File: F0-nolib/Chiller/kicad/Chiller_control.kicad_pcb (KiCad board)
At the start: 2 copper layers, 62 x 60.5 mm, 57 parts, among them J1 DB9_Female, J2 12VIN, J3 Ext. devices, J4 Tsens, J5 Cooler, J6 Heater, J7 Pump, Q1 SI2300, Q2 SI2300, Q3 SI2300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

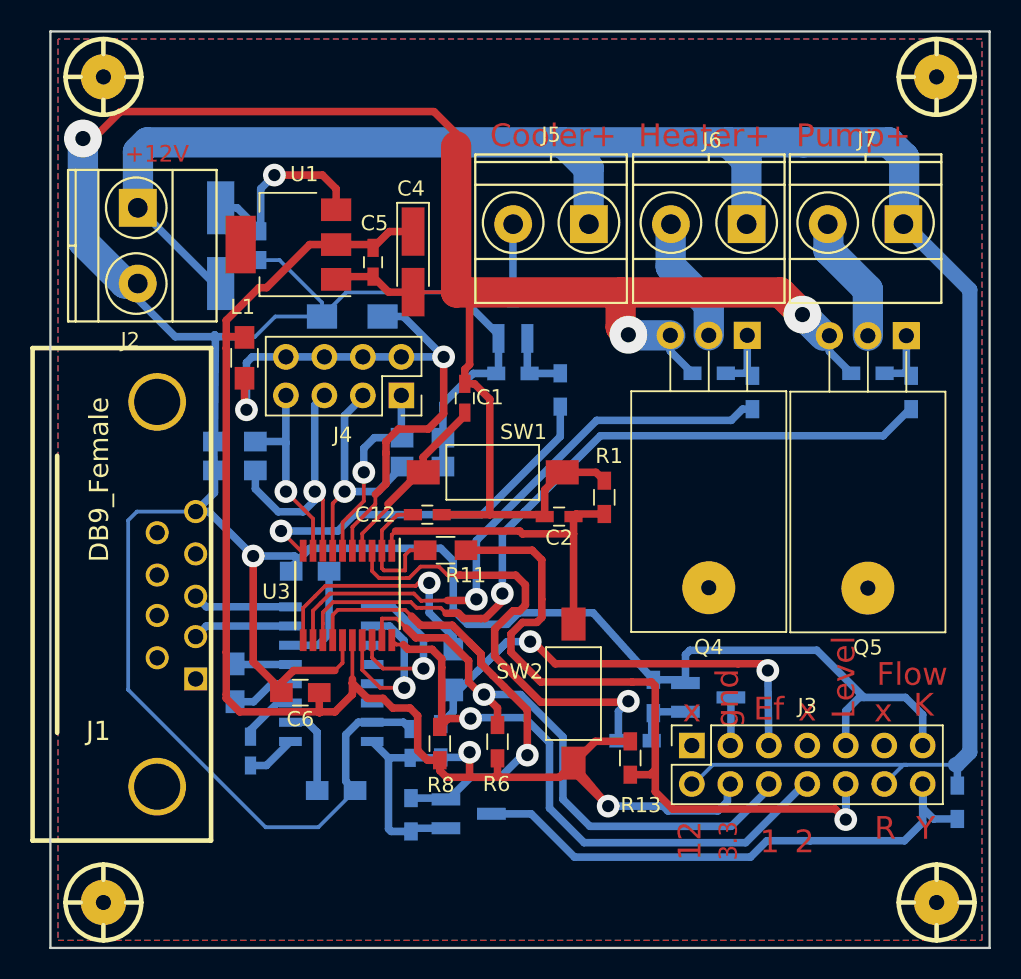
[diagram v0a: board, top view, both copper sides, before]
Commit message: Change chiller schematics: fix bugs, prepare for manufacture production
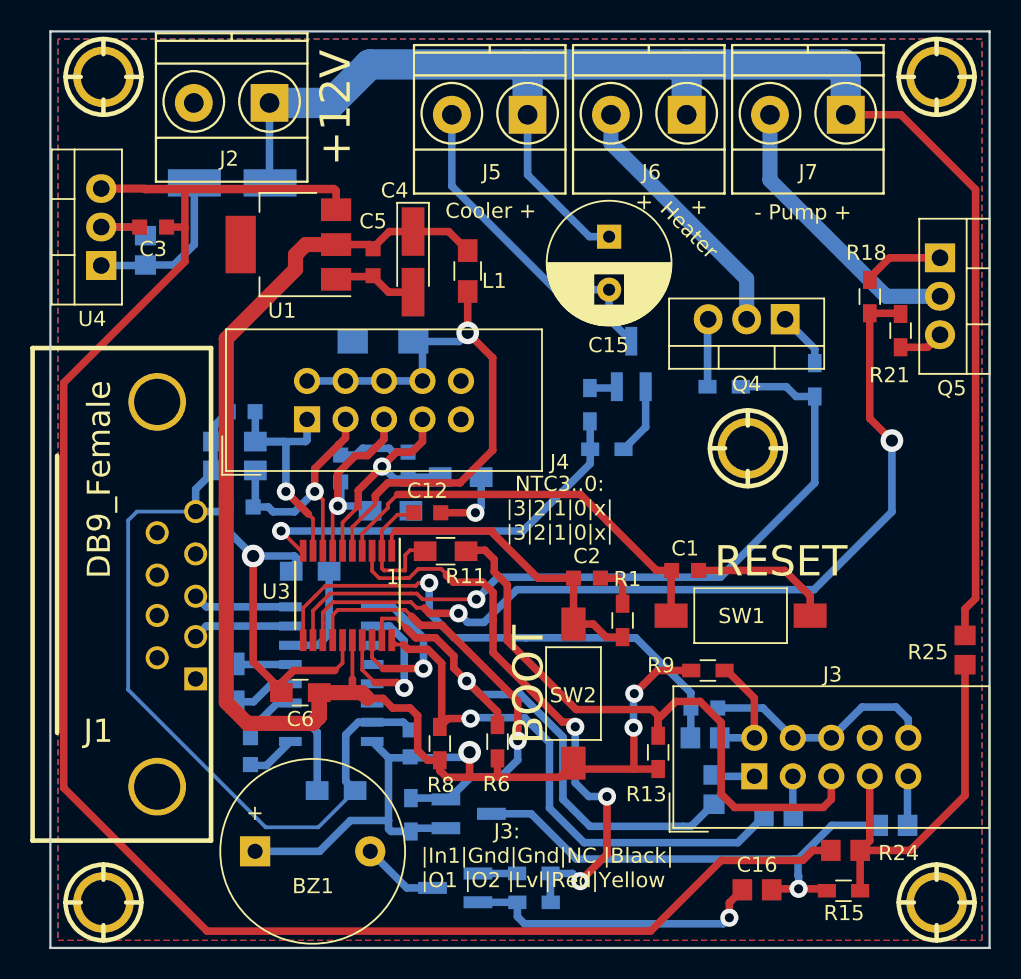
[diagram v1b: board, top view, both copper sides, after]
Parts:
- added BZ1: Buzzer, Buzzer_Beeper:Buzzer_12x9.5RM7.6, F.Cu at (55.9, 88.2)
- added C14: 1u, Capacitor_SMD:C_0805_2012Metric_Pad1.29x1.40mm_HandSolder, B.Cu at (48.6, 48.5)
- added C15: 100u, Capacitor_THT:CP_Radial_D8.0mm_P3.50mm, F.Cu at (79.2, 47.6)
- added C16: 1u, Capacitor_SMD:C_0805_2012Metric_Pad1.29x1.40mm_HandSolder, F.Cu at (89.0, 90.7)
- added C17: 0.1, Capacitor_SMD:C_0603_1608Metric_Pad0.99x1.00mm_HandSolder, B.Cu at (66.0, 62.7)
- added C18: 0.1, Capacitor_SMD:C_0603_1608Metric_Pad0.99x1.00mm_HandSolder, B.Cu at (55.0, 59.1)
- added C19: 0.1, Capacitor_SMD:C_0603_1608Metric_Pad0.99x1.00mm_HandSolder, B.Cu at (61.5, 62.9)
- added C20: 0.1, Capacitor_SMD:C_0603_1608Metric_Pad0.99x1.00mm_HandSolder, B.Cu at (54.8, 65.4)
- added C21: 0.1, Capacitor_SMD:C_0603_1608Metric_Pad0.99x1.00mm_HandSolder, B.Cu at (85.5, 78.7)
- added R22: 220, Resistor_SMD:R_0805_2012Metric_Pad1.29x1.40mm_HandSolder, B.Cu at (86.2, 84.1)
- added R23: 220, Resistor_SMD:R_0805_2012Metric_Pad1.29x1.40mm_HandSolder, B.Cu at (90.4, 85.8)
- added R24: 0, Resistor_SMD:R_0805_2012Metric_Pad1.29x1.40mm_HandSolder, F.Cu at (94.8, 88.1)
- added R25: 0, Resistor_SMD:R_0805_2012Metric_Pad1.29x1.40mm_HandSolder, F.Cu at (102.7, 74.9)
- added R26: 220, Resistor_SMD:R_0805_2012Metric_Pad1.29x1.40mm_HandSolder, B.Cu at (98.0, 86.4)
- added U4: L7805, TO_SOT_Packages_THT:TO-220-3_Vertical, F.Cu at (45.7, 49.5)
- added hole_3mm: Val**, modules:hole_3mm, F.Cu at (88.4, 61.5)
- C1, C12, C2, C5, C8, C9: footprint Capacitor_SMD.pretty:C_0603_HandSoldering -> Capacitor_SMD:C_0603_1608Metric_Pad0.99x1.00mm_HandSolder
- C3: footprint Capacitor_SMD.pretty:C_0603_HandSoldering -> Capacitor_SMD:C_0603_1608Metric_Pad0.99x1.00mm_HandSolder; moved to F.Cu
- J3: value Ext. devices -> DC3-10P; footprint Connector_PinSocket_2.54mm:PinSocket_2x07_P2.54mm_Vertical -> Connector_IDC:IDC-Header_2x05_P2.54mm_Vertical
- J4: value Tsens -> DC3-10P; footprint Connector_PinSocket_2.54mm:PinSocket_2x04_P2.54mm_Vertical -> Connector_IDC:IDC-Header_2x05_P2.54mm_Vertical
- Q4, Q5: footprint TO_SOT_Packages_THT:TO-220_Horizontal -> TO_SOT_Packages_THT:TO-220-3_Vertical
- R11: value 47 -> 220
- R15, R18, R21, R9: moved to F.Cu
- R7: value 47 -> 220; footprint Resistors_SMD.pretty:R_0805_HandSoldering -> Resistor_SMD:R_0805_2012Metric_Pad1.29x1.40mm_HandSolder
- moved Q1 20.9 mm to (69.1, 90.6), turned to 180 degrees
- moved SW1 18.9 mm to (87.9, 72.6)
- moved C1 18.5 mm to (84.3, 69.6), turned to 0 degrees
- moved R9 18.2 mm to (85.8, 76.2), turned to 0 degrees
- moved R7 17.2 mm to (85.6, 80.7), turned to 180 degrees
- moved L1 15.8 mm to (69.9, 49.8)
- moved R12 15.7 mm to (74.3, 91.5), turned to 0 degrees
- moved J2 11.1 mm to (56.8, 38.7), turned to 180 degrees
- moved R10 11.0 mm to (74.3, 89.6), turned to 0 degrees
- moved R15 9.52 mm to (94.7, 90.8), turned to 180 degrees
- moved Q3 8.44 mm to (80.7, 56.0)
- moved J5 8.28 mm to (73.9, 39.5)
- moved J6 8.24 mm to (84.4, 39.5)
- moved R1 8.22 mm to (80.1, 72.9)
- moved J7 8.17 mm to (94.9, 39.5)
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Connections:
- C3 pad 1: Net-(C3-Pad1) -> +5V
- D1 pad 1: Net-(C3-Pad1) -> Net-(C14-Pad1)
- J3 pad 1: (no net) -> /Out1
- J3 pad 10: /W.levl -> GND
- J3 pad 2: +12V -> /IN
- J3 pad 3: /Alrm -> /Out2
- J3 pad 4: +3V3 -> GND
- J3 pad 5: /EF -> /W.levl
- J3 pad 6: /DigOut1 -> GND
- J3 pad 7: (no net) -> /Red
- J3 pad 8: /DigOut2 -> (no net)
- J3 pad 9: GND -> /Yellow
- J4 pad 1: /ADC0 -> /ADC3
- J4 pad 3: /ADC1 -> /ADC2
- J4 pad 5: /ADC2 -> /ADC1
- J4 pad 7: /ADC3 -> /ADC0
- Q1 pad 3: /Alrm -> Net-(BZ1-Pad2)
- Q2 pad 3: /Yellow -> Net-(C16-Pad2)
- R12 pad 2: Net-(Q1-Pad1) -> /DigOut0
- R15 pad 1: +12V -> /Red
- R15 pad 2: /Yellow -> Net-(C16-Pad2)
- R19 pad 2: Net-(Q3-Pad1) -> /Tim14Ch1
- R20 pad 2: Net-(Q4-Pad1) -> /TIM16_Ch1
- R21 pad 2: Net-(Q5-Pad1) -> /TIM17_Ch1
- R7 pad 1: /EF -> /IN
- R9 pad 2: /EF -> /IN
- U1 pad 3: Net-(C3-Pad1) -> +5V
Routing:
- net GND: track 309.7 -> 157.0 mm, vias 4 -> 3
- net +5V: track 0.00 -> 133.2 mm
- net /Yellow: track 37.3 -> 3.26 mm
- net Net-(C16-Pad2): track 0.00 -> 33.4 mm, vias 0 -> 1
- net /EF: track 33.2 -> 0.00 mm, vias 2 -> 0
- net +12V: track 138.2 -> 105.8 mm
- net /Red: track 0.00 -> 24.9 mm
- net /DigIn1: track 16.2 -> 36.5 mm
- net Net-(C15-Pad2): track 4.55 -> 21.9 mm
- net /NRST: track 13.9 -> 27.9 mm
- net Net-(C3-Pad1): track 13.2 -> 0.00 mm, vias 1 -> 0
- net Net-(C14-Pad1): track 0.00 -> 10.8 mm
- net /TIM16_Ch1: track 39.1 -> 49.9 mm
- net Net-(J7-Pad2): track 8.44 -> 18.7 mm
- net /TIM17_Ch1: track 49.7 -> 59.0 mm, vias 1 -> 2
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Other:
- net class Default: via_dia 1.5 -> 1.2; via_drill 0.8 -> 0.6
- board text added: "+"
- board text added: "- Pump +"
- board text added: "BOOT"
- board text added: "Cooler +"
- board text added: "Heater"
- board text added: "J3: |In1|Gnd|Gnd|NC |Black| |O1 |O2 |Lvl|Red|Yellow"
- board text added: "NTC3..0: |3|2|1|0|x| |3|2|1|0|x|"
- board text added: "RESET"
- board text removed: "12"
- board text removed: "2"
- board text removed: "3.3"
- board text removed: "Cooler+"
- board text removed: "Ef"
- board text removed: "Flow"
- board text removed: "Heater+"
- board text removed: "K"
- board text removed: "Level"
- board text removed: "Pump+"
- board text removed: "R"
- board text removed: "Y"
- board text removed: "gnd"
- board text removed: "x"
